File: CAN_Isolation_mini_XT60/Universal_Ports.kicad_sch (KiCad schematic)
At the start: 21 parts, among them J10 Conn_01x04_Pin, J11 Conn_01x04_Pin, J12 Conn_01x04_Pin, J13 Conn_01x04_Pin, J14 Conn_01x04_Pin, J15 Conn_01x04_Pin, J16 Conn_01x04_Pin, J17 Conn_01x04_Pin, J18 S2B-XH-A, J19 S2B-XH-A, J2 Conn_01x04_Pin, J20 S5B-XH-A, J21 XT60PW-F, J22 XT60PW-F, J3 Conn_01x04_Pin, J4 Conn_01x04_Pin, J5 Conn_01x04_Pin, J6 Conn_01x04_Pin, J7 Conn_01x04_Pin, J8 Conn_01x04_Pin, J9 Conn_01x04_Pin

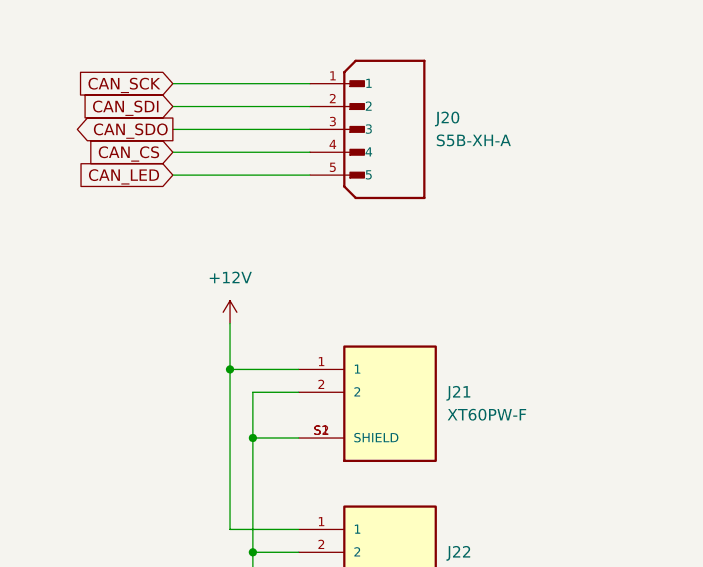
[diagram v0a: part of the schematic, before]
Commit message: Add diode for servo line.
Add diode for servo line.
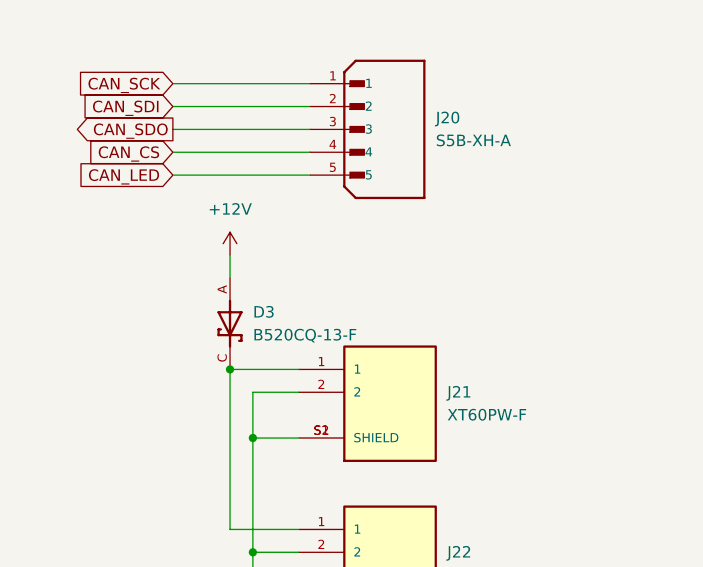
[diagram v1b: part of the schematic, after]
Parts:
- added D3: B520CQ-13-F, CAN_Isolation:DIOM7959X250N, symbol B520CQ-13-F:B520CQ-13-F
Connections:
- net +12V: now also D3.A; no longer J21.1, J22.1
- new net: D3.C, J21.1, J22.1

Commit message: Fix XT60 line.
Fix XT60 line.
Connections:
- net +12V: now also J22.1
- net at D3.C, J21.1: no longer J22.1
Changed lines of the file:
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@@
-	)
-	(junction
-		(at 54.61 144.78)
-		(diameter 0)
-		(color 0 0 0 0)
 	)
 	(junction
@@
 	)
 	(junction
-		(at 57.15 78.74)
+		(at 143.51 31.75)
 		(diameter 0)
 		(color 0 0 0 0)
 	)
 	(junction
-		(at 143.51 31.75)
+		(at 57.15 78.74)
 		(diameter 0)
 		(color 0 0 0 0)
@@
 	)
 	(junction
+		(at 54.61 133.35)
+		(diameter 0)
+		(color 0 0 0 0)
+	)
+	(junction
 		(at 60.96 50.8)
 		(diameter 0)
@@
 	(wire
 		(pts
+			(xy 57.15 78.74) (xy 57.15 88.9)
+		)
+		(stroke
+			(width 0)
+			(type default)
+		)
+	)
+	(wire
+		(pts
 			(xy 57.15 147.32) (xy 57.15 152.4)
 		)
@@
 	(wire
 		(pts
+			(xy 46.99 162.56) (xy 46.99 133.35)
+		)
+		(stroke
+			(width 0)
+			(type default)
+		)
+	)
+	(wire
+		(pts
+			(xy 46.99 133.35) (xy 54.61 133.35)
+		)
+		(stroke
+			(width 0)
+			(type default)
+		)
+	)
+	(wire
+		(pts
+			(xy 46.99 162.56) (xy 62.23 162.56)
+		)
+		(stroke
+			(width 0)
+			(type default)
+		)
+	)
+	(wire
+		(pts
 			(xy 127 50.8) (xy 127 53.34)
 		)
@@
 	(wire
 		(pts
-			(xy 57.15 78.74) (xy 57.15 88.9)
-		)
-		(stroke
-			(width 0)
-			(type default)
-		)
-	)
-	(wire
-		(pts
 			(xy 110.49 45.72) (xy 113.03 45.72)
 		)
@@
 	(wire
 		(pts
-			(xy 54.61 132.08) (xy 54.61 134.62)
+			(xy 54.61 132.08) (xy 54.61 133.35)
 		)
 		(stroke
@@
 	(wire
 		(pts
+			(xy 54.61 133.35) (xy 54.61 134.62)
+		)
+		(stroke
+			(width 0)
+			(type default)
+		)
+	)
+	(wire
+		(pts
 			(xy 127 29.21) (xy 127 31.75)
 		)
@@
 	(wire
 		(pts
-			(xy 62.23 162.56) (xy 54.61 162.56)
-		)
-		(stroke
-			(width 0)
-			(type default)
-		)
-	)
-	(wire
-		(pts
 			(xy 58.42 91.44) (xy 62.23 91.44)
 		)
@@
 		(pts
 			(xy 110.49 50.8) (xy 110.49 53.34)
-		)
-		(stroke
-			(width 0)
-			(type default)
-		)
-	)
-	(wire
-		(pts
-			(xy 54.61 162.56) (xy 54.61 144.78)
 		)
 		(stroke
@@
 	)
 	(symbol
+		(lib_id "power:+5VP")
+		(at 147.32 24.13 0)
+		(unit 1)
+		(exclude_from_sim no)
+		(in_bom yes)
+		(on_board yes)
+		(dnp no)
+		(fields_autoplaced yes)
+		(property "Reference" "#PWR027"
+			(at 147.32 27.94 0)
+			(effects
+				(font
+					(size 1.27 1.27)
+				)
+				(hide yes)
+			)
+		)
+		(property "Value" "+5VP"
+			(at 147.32 19.05 0)
+			(effects
+				(font
+					(size 1.27 1.27)
+				)
+			)
+		)
+		(property "Footprint" ""
+			(at 147.32 24.13 0)
+			(effects
+				(font
+					(size 1.27 1.27)
+				)
+				(hide yes)
+			)
+		)
+		(property "Datasheet" ""
+			(at 147.32 24.13 0)
+			(effects
+				(font
+					(size 1.27 1.27)
+				)
+				(hide yes)
+			)
+		)
+		(property "Description" "Power symbol creates a global label with name \"+5VP\""
+			(at 147.32 24.13 0)
+			(effects
+				(font
+					(size 1.27 1.27)
+				)
+				(hide yes)
+			)
+		)
+		(pin "1"
+		)
+		(instances
+			(project "CAN_Isolation_mini"
+				(path "/d188d587-a283-4d42-bf18-6e85dcc02a49/54dda61f-9174-4ddd-af5e-6bc53d2182b0"
+					(reference "#PWR027")
+					(unit 1)
+				)
+			)
+		)
+	)
+	(symbol
 		(lib_id "Connector:Conn_01x04_Pin")
 		(at 39.37 48.26 0)
@@
 					(unit 1)
 				)
-			)
-		)
-	)
-	(symbol
-		(lib_id "power:+5VP")
-		(at 147.32 24.13 0)
-		(unit 1)
-		(exclude_from_sim no)
-		(in_bom yes)
-		(on_board yes)
-		(dnp no)
-		(fields_autoplaced yes)
-		(property "Reference" "#PWR027"
-			(at 147.32 27.94 0)
-			(effects
-				(font
-					(size 1.27 1.27)
-				)
-				(hide yes)
-			)
-		)
-		(property "Value" "+5VP"
-			(at 147.32 19.05 0)
-			(effects
-				(font
-					(size 1.27 1.27)
-				)
-			)
-		)
-		(property "Footprint" ""
-			(at 147.32 24.13 0)
-			(effects
-				(font
-					(size 1.27 1.27)
-				)
-				(hide yes)
-			)
-		)
-		(property "Datasheet" ""
-			(at 147.32 24.13 0)
-			(effects
-				(font
-					(size 1.27 1.27)
-				)
-				(hide yes)
-			)
-		)
-		(property "Description" "Power symbol creates a global label with name \"+5VP\""
-			(at 147.32 24.13 0)
-			(effects
-				(font
-					(size 1.27 1.27)
-				)
-				(hide yes)
-			)
-		)
-		(pin "1"
-		)
-		(instances
-			(project "CAN_Isolation_mini"
-				(path "/d188d587-a283-4d42-bf18-6e85dcc02a49/54dda61f-9174-4ddd-af5e-6bc53d2182b0"
-					(reference "#PWR027")
-					(unit 1)
-				)
